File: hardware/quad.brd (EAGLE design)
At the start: 132.1 x 53.3 mm, 18 parts, among them U101 STM32F427VGT6, X101 24MHz

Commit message: Add USB-UART, BNO055
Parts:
- removed J301, J302: (no value), quad:1X50
- added C211, C401, C402, C403, C404: 100nF, quad:C0603
- added C212, C213, C405, C406: 10uF, quad:C0603
- added ESC1, ESC2, ESC3, ESC4: AFRO_ESC, quad:AFRO_ESC
- added IC1: BN055, quad:LGA-28_3.80X5.20/0.5
- added MOT1, MOT2, MOT3, MOT4: MOTOR, quad:MOTOR
- added R101, R401: 10k, quad:R0603
- added R402, R403: 270, quad:R0603
- added RXLED, TXLED: LED, quad:LED-0603
- added U201, U403: LD1117, quad:SOT223
- added U401: FT232R, quad:SSOP28
- added U402: USB-MICROB", quad:USB-B-MICRO-SMD_V03
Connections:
- new net GND_IO: IC1.25
- new net MOT1_1: ESC1.MOT1, MOT1.MOT1
- new net MOT1_2: ESC1.MOT2, MOT1.MOT2
- new net MOT1_3: ESC1.MOT3, MOT1.MOT3
- new net MOT2_1: ESC2.MOT1, MOT2.MOT1
- new net MOT_2_2: ESC2.MOT2, MOT2.MOT2
- new net MOT_2_3: ESC2.MOT3, MOT2.MOT3
- new net MOT_3_1: ESC3.MOT1, MOT3.MOT1
- new net MOT_3_2: ESC3.MOT2, MOT3.MOT2
- new net MOT_3_3: ESC3.MOT3, MOT3.MOT3
- new net MOT_4_1: ESC4.MOT1, MOT4.MOT1
- new net MOT_4_2: ESC4.MOT2, MOT4.MOT2
- new net MOT_4_3: ESC4.MOT3, MOT4.MOT3
- new net N$10: R402.2, RXLED.C
- new net N$11: R403.2, TXLED.C
- new net N$2: R401.1, U401.19
- new net N$5: C401.1, U401.17
- new net N$8: R403.1, U401.23
- new net N$9: R402.1, U401.22
- new net PWM1: ESC1.PWM
- new net PWM2: ESC2.PWM
- new net PWM3: ESC3.PWM
- new net PWM4: ESC4.PWM
- new net USBDM: U401.16, U402.D-
- new net USBDP: U401.15, U402.D+
- new net VBATT: C213.1, ESC1.VBATT, ESC2.VBATT, ESC3.VBATT, ESC4.VBATT, U201.3
- new net VBUS: C402.2, C403.1, C404.1, C405.1, R401.2, U401.20, U403.3
- new net VDD: IC1.3
- new net VDDIO: IC1.28
- net BOOT0: now also U401.2; no longer J302.44
- net BOOT1: now also R101.1; no longer J301.37
- net CAN1_RX: no longer J302.31
- net CAN1_TX: no longer J302.32
- net CAN2_RX: no longer J302.41
- net CAN2_TX: no longer J302.42
- net GND: now also C211.2, C212.2, C213.2, C401.2, C402.1, C403.2, C404.2, C405.2, C406.2, ESC1.GND, ESC1.PWM_GND, ESC2.GND, ESC2.PWM_GND, ESC3.GND, ESC3.PWM_GND, ESC4.GND, ESC4.PWM_GND, IC1.2, R101.2, U201.1, U401.18, U401.21, U401.25, U401.26, U401.7, U402.GND, U403.1; no longer J301.10, J301.11, J301.12, J301.13, J301.19, J301.20, J301.21, J301.22, J301.27, J301.28, J301.49, J301.6, J302.23, J302.24, J302.25, J302.49, J302.50
- net I2C1_SCL: no longer J302.45
- net I2C1_SDA: no longer J302.46
- net I2C2_SCL: no longer J301.47
- net I2C2_SDA: no longer J301.48
- net I2C3_SCL: no longer J302.17
- net I2C3_SDA: no longer J302.16
- net JTCK-SWCLK: no longer J302.26
- net JTDI: no longer J302.27
- net JTDO/TRACESWO: no longer J302.39
- net JTMS-SWDIO: no longer J302.22
- net NJTRST: no longer J302.40
- net NRST: now also U401.3; no longer J301.14
- net PA2: no longer J301.25
- net PA3: no longer J301.26
- net PA4: no longer J301.29
- net PB0: no longer J301.35
- net PB1: no longer J301.36
- net PB12: no longer J302.1
- net PB7: no longer J302.43
- net PC0: no longer J301.15
- net PC1: no longer J301.16
- net PC13: no longer J301.7
- net PC14: no longer J301.8
- net PC15: no longer J301.9
- net PC2: no longer J301.17
- net PC3: no longer J301.18
- net PC4: no longer J301.33
- net PC5: no longer J301.34
- net PC8: no longer J302.15
- net PD10: no longer J302.7
- net PD13: no longer J302.10
- net PD14: no longer J302.11
- net PD15: no longer J302.12
- net PD2: no longer J302.33
- net PD7: no longer J302.38
- net PE10: no longer J301.41
- net PE11: no longer J301.42
- net PE15: no longer J301.46
- net PE2: no longer J301.1
- net PE3: no longer J301.2
- net PE4: no longer J301.3
- net PE5: no longer J301.4
- net PE6: no longer J301.5
- net PE9: no longer J301.40
- net SPI1_MISO: no longer J301.31
- net SPI1_MOSI: no longer J301.32
- net SPI1_SCK: no longer J301.30
- net SPI2_MISO: no longer J302.3
- net SPI2_MOSI: no longer J302.4
- net SPI2_SCK: no longer J302.2
- net SPI3_MISO: no longer J302.29
- net SPI3_MOSI: no longer J302.30
- net SPI3_SCK: no longer J302.28
- net SPI4_MISO: no longer J301.44
- net SPI4_MOSI: no longer J301.45
- net SPI4_SCK: no longer J301.43
- net UART4_RX: no longer J301.24
- net UART4_TX: no longer J301.23
- net UART7_RX: no longer J301.38
- net UART7_TX: no longer J301.39
- net UART8_RX: no longer J302.47
- net UART8_TX: no longer J302.48
- net USART1_CTS: no longer J302.20
- net USART1_RTS: no longer J302.21
- net USART1_RX: now also U401.1; no longer J302.19
- net USART1_TX: now also U401.5; no longer J302.18
- net USART2_CTS: no longer J302.34
- net USART2_RTS: no longer J302.35
- net USART2_RX: no longer J302.37
- net USART2_TX: no longer J302.36
- net USART3_CTS: no longer J302.8
- net USART3_RTS: no longer J302.9
- net USART3_RX: no longer J302.6
- net USART3_TX: no longer J302.5
- net USART6_RX: no longer J302.14
- net USART6_TX: no longer J302.13
- net VDD_3V3: now also C211.1, C212.1, C406.1, RXLED.A, TXLED.A, U201.2, U201.4, U401.4, U403.2, U403.4; no longer J301.50
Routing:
- net VDD_3V3: track 167.9 -> 99.9 mm
- net PB12: track 61.8 -> 0.00 mm
- net PE2: track 61.2 -> 0.00 mm
- net SPI2_SCK: track 59.4 -> 0.00 mm
- net PE3: track 58.9 -> 0.00 mm
- net SPI2_MISO: track 57.1 -> 0.00 mm
- net UART8_TX: track 57.1 -> 0.00 mm
- net I2C2_SDA: track 56.6 -> 0.00 mm
- net PE4: track 56.6 -> 0.00 mm
- net SPI2_MOSI: track 54.8 -> 0.00 mm
- net UART8_RX: track 54.8 -> 0.00 mm
- net BOOT0: track 54.3 -> 0.00 mm, vias 2 -> 0
- net I2C2_SCL: track 54.2 -> 0.00 mm
- net PE5: track 54.2 -> 0.00 mm
- net PC14: track 53.1 -> 0.00 mm, vias 1 -> 0
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- removed copper zone on layer 1, net GND
- removed copper zone on layer 16, net GND
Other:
- board outline removed
- board text removed: "BOOT0"
- board text removed: "BOOT1"
- board text removed: "CAN1_RX"
- board text removed: "CAN1_TX"
- board text removed: "CAN2_RX"
- board text removed: "CAN2_TX"
- board text removed: "GND"
- board text removed: "I2C1_SCL"
- board text removed: "I2C1_SDA"
- board text removed: "I2C2_SCL"
- board text removed: "I2C2_SDA"
- board text removed: "I2C3_SCL"
- board text removed: "I2C3_SDA"
- board text removed: "JTCK-SWCLK"
- board text removed: "JTDI"
- board text removed: "JTDO-TRACESWO"
- board text removed: "JTMS-SWDIO"
- board text removed: "NJTRST"
- board text removed: "NRST"
- board text removed: "PA2"
- board text removed: "PA3"
- board text removed: "PA4"
- board text removed: "PB0"
- board text removed: "PB1"
- board text removed: "PB12"
- board text removed: "PB7"
- board text removed: "PC0"
- board text removed: "PC1"
- board text removed: "PC13"
- board text removed: "PC14"
- board text removed: "PC15"
- board text removed: "PC2"
- board text removed: "PC3"
- board text removed: "PC4"
- board text removed: "PC5"
- board text removed: "PC8"
- board text removed: "PD10"
- board text removed: "PD13"
- board text removed: "PD14"
- board text removed: "PD15"
- board text removed: "PD2"
- board text removed: "PD7"
- board text removed: "PE10"
- board text removed: "PE11"
- board text removed: "PE15"
- board text removed: "PE2"
- board text removed: "PE3"
- board text removed: "PE4"
- board text removed: "PE5"
- board text removed: "PE6"
- board text removed: "PE9"
- board text removed: "SPI1_MISO"
- board text removed: "SPI1_MOSI"
- board text removed: "SPI1_SCK"
- board text removed: "SPI2_MISO"
- board text removed: "SPI2_MOSI"
- board text removed: "SPI2_SCK"
- board text removed: "SPI3_MISO"
- board text removed: "SPI3_MOSI"
- board text removed: "SPI3_SCK"
- board text removed: "SPI4_MISO"
- board text removed: "SPI4_MOSI"
- board text removed: "SPI4_SCK"
- board text removed: "UART4_RX"
- board text removed: "UART4_TX"
- board text removed: "UART7_RX"
- board text removed: "UART7_TX"
- board text removed: "UART8_RX"
- board text removed: "UART8_TX"
- board text removed: "USART1_CTS"
- board text removed: "USART1_RTS"
- board text removed: "USART1_RX"
- board text removed: "USART1_TX"
- board text removed: "USART2_CTS"
- board text removed: "USART2_RTS"
- board text removed: "USART2_RX"
- board text removed: "USART2_TX"
- board text removed: "USART3_CTS"
- board text removed: "USART3_RTS"
- board text removed: "USART3_RX"
- board text removed: "USART3_TX"
- board text removed: "USART6_RX"
- board text removed: "USART6_TX"
- board text removed: "VDD_3V3"

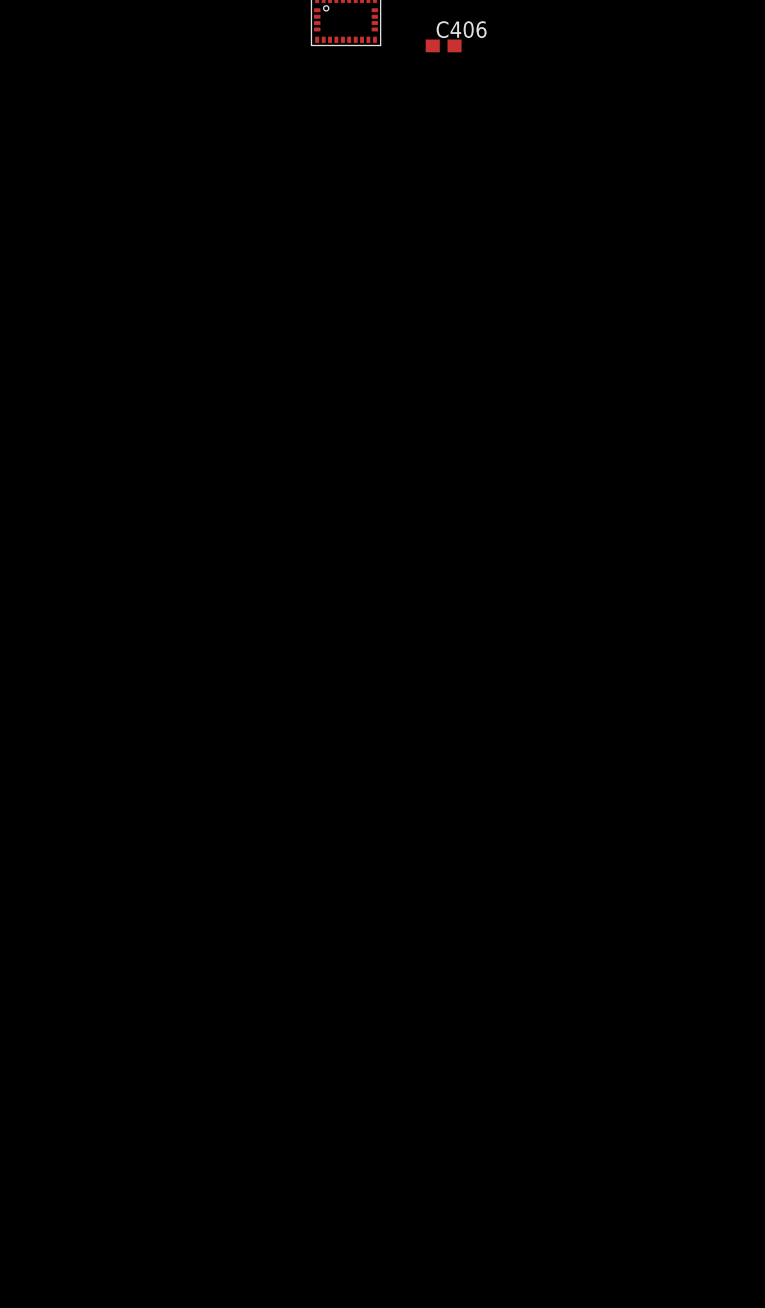
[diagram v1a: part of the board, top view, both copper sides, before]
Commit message: Wire BNO055, Added XBEE
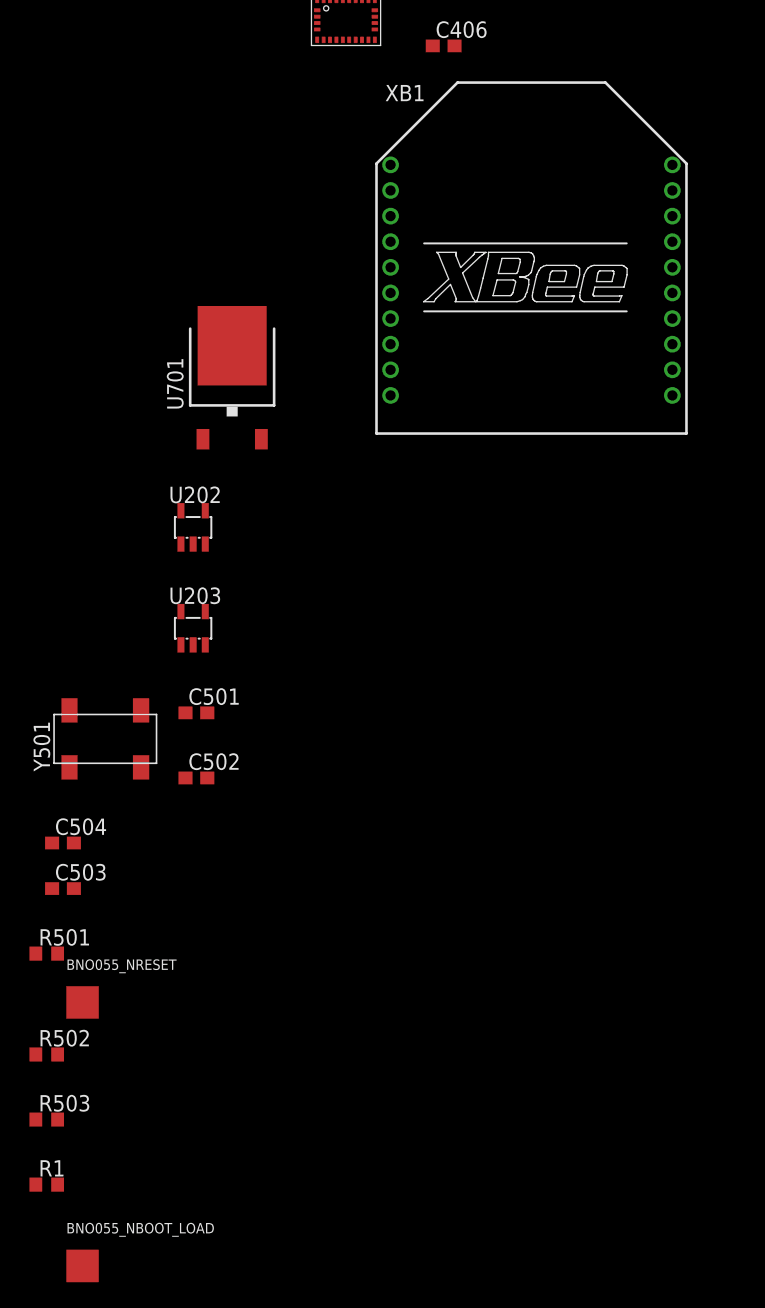
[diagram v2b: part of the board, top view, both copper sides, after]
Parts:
- added BNO055_NBOOT_LOAD, BNO055_NRESET: TESTPAD, quad:TESTPAD
- added C501, C502: 0.1uF, quad:C0603
- added C503, C504: 22pF, quad:C0603
- added R1, R501, R502, R503: 10k, quad:R0603
- added U202, U203: SN74AHC1G32DBVR, quad:SOT23-5L
- added U701: AOD4189, quad:TO252
- added XB1: XBEE, quad:XBEE
- added Y501: 32.768kHz, quad:ABS25
- C404: value 100nF -> 4.7uF
- IC1: value BN055 -> BNO055
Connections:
- removed net GND_IO: IC1.25
- removed net VDD: IC1.3
- removed net VDDIO: IC1.28
- new net FT232_DTR: U203.2, U401.2
- new net FT232_RTS: U202.2, U401.3
- new net N$12: IC1.17, R501.1
- new net N$13: BNO055_NRESET.P$1, IC1.11
- new net N$14: IC1.6, R503.1
- new net N$15: IC1.5, R502.1
- new net N$16: BNO055_NBOOT_LOAD.P$1, IC1.4, R1.1
- new net N$3: U701.3
- new net N$4: C501.2, IC1.9
- new net N$6: C504.2, IC1.27, Y501.4
- new net N$7: C503.2, IC1.26, Y501.1
- new net XBEE_DIO0: U202.1, XB1.20
- new net XBEE_DIO1: U203.1, XB1.19
- new net XBEE_DIO4: XB1.11
- net BOOT0: now also U203.4; no longer U401.2
- net GND: now also C501.1, C502.1, C503.1, C504.1, IC1.10, IC1.15, IC1.16, IC1.18, IC1.25, R501.2, R502.2, R503.2, U202.3, U203.3, XB1.10
- net I2C1_SCL: now also IC1.19
- net I2C1_SDA: now also IC1.20
- net NRST: now also U202.4; no longer U401.3
- net PB12: now also IC1.14
- net USART3_RX: now also XB1.2
- net USART3_TX: now also XB1.3
- net VBATT: now also U701.2
- net VDD_3V3: now also C502.2, IC1.28, IC1.3, R1.2, U202.5, U203.5, XB1.1

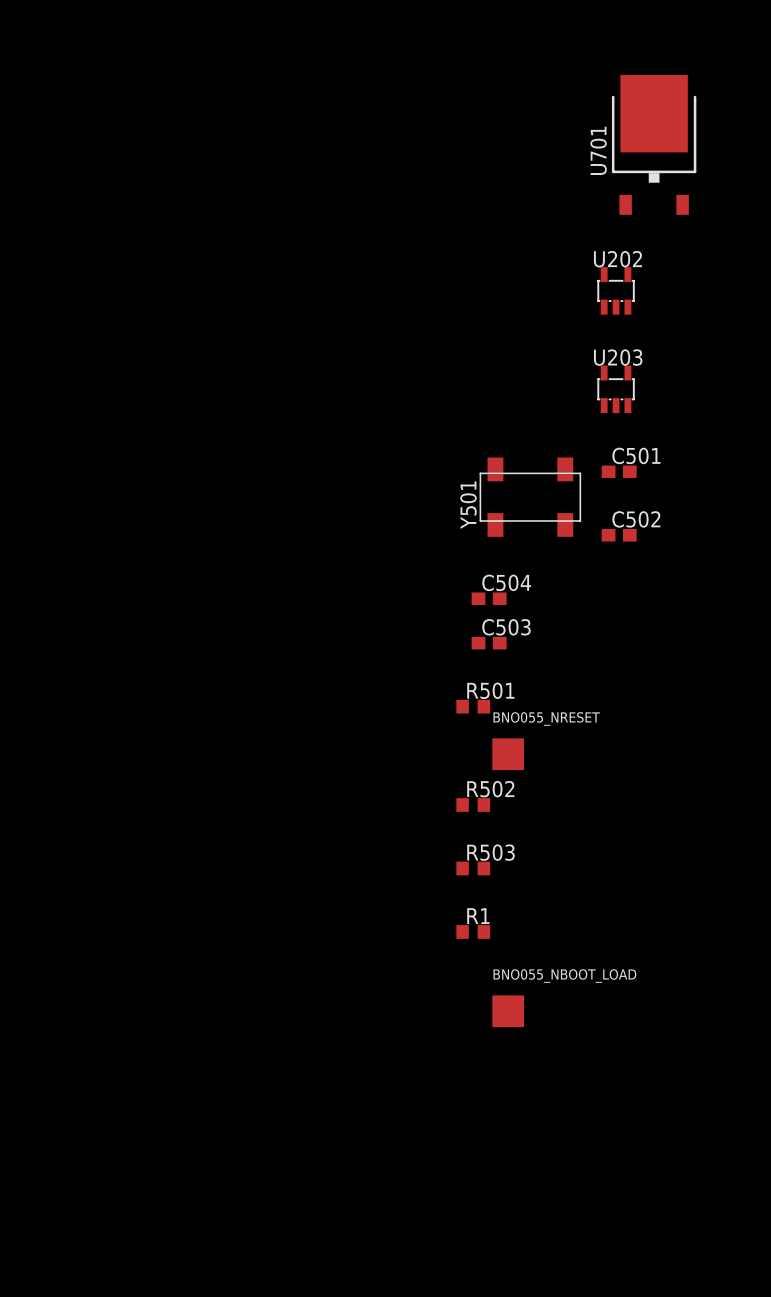
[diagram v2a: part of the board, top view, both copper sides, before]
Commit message: Add power connectors, finish BNO055
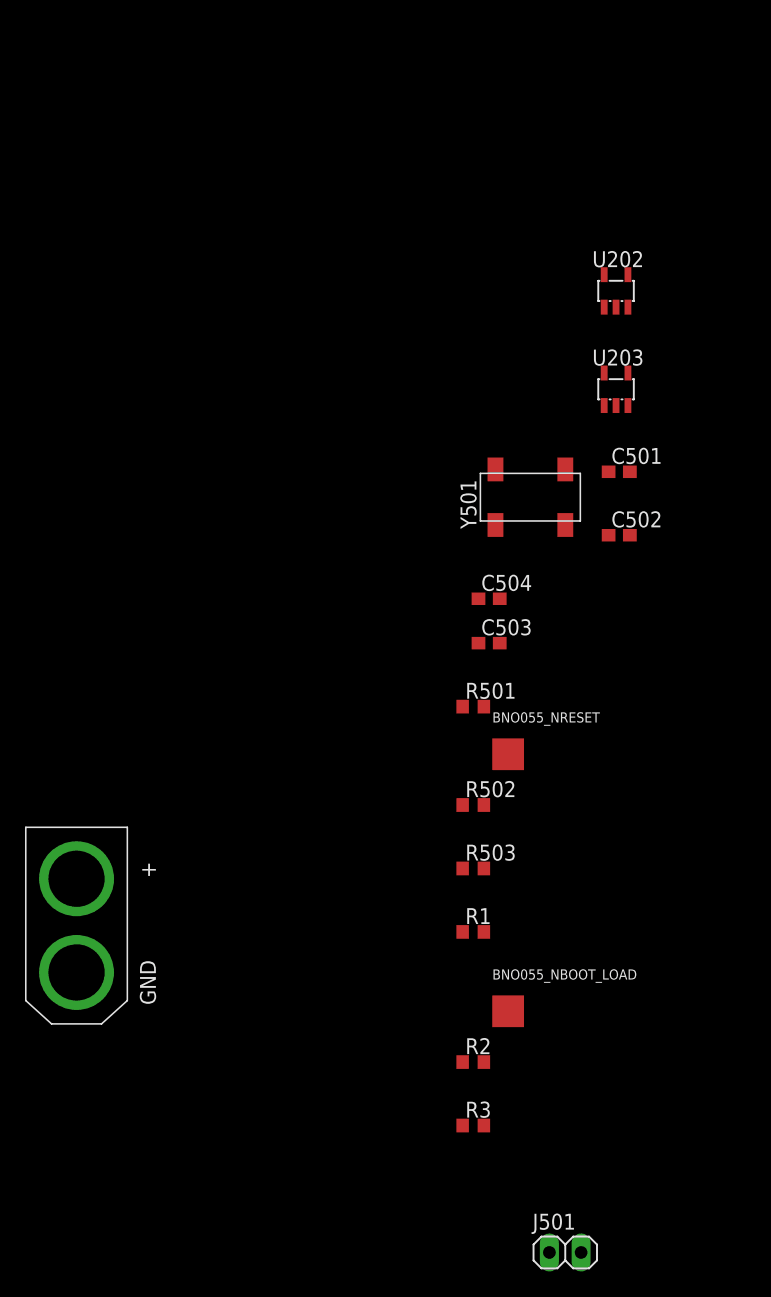
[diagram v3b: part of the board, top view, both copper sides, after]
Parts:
- removed U701: AOD4189, quad:TO252
- added J501: I2C_TEST, quad:1X02
- added R2, R3: 10k, quad:R0603
- added U$1: XT60, quad:XT60
- U202: value SN74AHC1G32DBVR -> AND_GATE
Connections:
- net SPI3_MOSI renamed PC12
- net USART3_CTS renamed PD11
- net USART3_RTS renamed PD12
- removed net SPI3_MISO: U101.79
- removed net SPI3_SCK: U101.78
- new net PD8: U101.55
- new net PD9: U101.56
- net GND: now also U$1.GND
- net I2C1_SCL: now also J501.2, R3.2
- net I2C1_SDA: now also J501.1, R2.2
- net N$3: now also U$1.PWR; no longer U701.3
- net USART3_RX: now also U101.79; no longer U101.56
- net USART3_TX: now also U101.78; no longer U101.55
- net VBATT: no longer U701.2
- net VDD_3V3: now also R2.1, R3.1
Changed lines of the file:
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@@
 <attribute name="OC_NEWARK" value="34R5507" x="-236.982" y="-274.32" size="1.778" layer="27" display="off"/>
 </element>
-<element name="U701" library="quad" package="TO252" value="AOD4189" x="-260.35" y="-281.94"/>
-<element name="U202" library="quad" package="SOT23-5L" value="SN74AHC1G32DBVR" x="-263.398" y="-293.624"/>
+<element name="U202" library="quad" package="SOT23-5L" value="AND_GATE" x="-263.398" y="-293.624"/>
 <element name="U203" library="quad" package="SOT23-5L" value="SN74AHC1G32DBVR" x="-263.398" y="-301.498"/>
 <element name="C501" library="quad" package="C0603" value="0.1uF" x="-263.144" y="-308.102"/>
@@
 <element name="R1" library="quad" package="R0603" value="10k" x="-274.828" y="-344.932"/>
 <element name="BNO055_NBOOT_LOAD" library="quad" package="TESTPAD" value="TESTPAD" x="-272.034" y="-351.282"/>
+<element name="R2" library="quad" package="R0603" value="10k" x="-274.828" y="-355.346"/>
+<element name="R3" library="quad" package="R0603" value="10k" x="-274.828" y="-360.426"/>
+<element name="J501" library="quad" package="1X02" value="I2C_TEST" x="-267.462" y="-370.586"/>
+<element name="U$1" library="quad" package="XT60" value="XT60" x="-306.578" y="-344.424"/>
 </elements>
 <signals>
@@
 <contactref element="R502" pad="2"/>
 <contactref element="R503" pad="2"/>
+<contactref element="U$1" pad="GND"/>
 <wire x1="-249.21" y1="-255.56" x2="-251.71" y2="-255.56" width="0" layer="19" extent="1-1"/>
 <wire x1="-249.21" y1="-254.75" x2="-249.21" y2="-255.56" width="0" layer="19" extent="1-1"/>
@@
 <wire x1="-273.978" y1="-334.772" x2="-273.978" y2="-326.898" width="0" layer="19" extent="1-1"/>
 <wire x1="-273.978" y1="-339.852" x2="-273.978" y2="-334.772" width="0" layer="19" extent="1-1"/>
+<wire x1="-306.578" y1="-348.174" x2="-273.978" y2="-339.852" width="0" layer="19" extent="1-1"/>
 <wire x1="-208.026" y1="91.186" x2="-223.68" y2="-167.946" width="0" layer="19" extent="1-1"/>
 <wire x1="-195.326" y1="95.631" x2="-208.026" y2="91.186" width="0" layer="19" extent="1-1"/>
@@
 <contactref element="U101" pad="95"/>
 <contactref element="IC1" pad="19"/>
+<contactref element="R3" pad="2"/>
+<contactref element="J501" pad="2"/>
+<wire x1="-273.978" y1="-360.426" x2="-249.21" y2="-253.25" width="0" layer="19" extent="1-1"/>
+<wire x1="-266.192" y1="-370.586" x2="-273.978" y2="-360.426" width="0" layer="19" extent="1-1"/>
 <wire x1="58.105128125" y1="30.290121875" x2="-249.21" y2="-253.25" width="0" layer="19" extent="1-1"/>
 </signal>
 <signal name="I2C1_SDA">
 <contactref element="U101" pad="96"/>
+<contactref element="J501" pad="1"/>
 <contactref element="IC1" pad="20"/>
+<contactref element="R2" pad="2"/>
+<wire x1="-273.978" y1="-355.346" x2="-249.21" y2="-252.44" width="0" layer="19" extent="1-1"/>
+<wire x1="-268.732" y1="-370.586" x2="-273.978" y2="-355.346" width="0" layer="19" extent="1-1"/>
 <wire x1="57.751575" y1="29.936565625" x2="-249.21" y2="-252.44" width="0" layer="19" extent="1-1"/>
 </signal>
@@
 <contactref element="U101" pad="66"/>
 </signal>
-<signal name="SPI3_SCK">
-<contactref element="U101" pad="78"/>
-</signal>
-<signal name="SPI3_MISO">
-<contactref element="U101" pad="79"/>
-</signal>
-<signal name="SPI3_MOSI">
+<signal name="PC12">
 <contactref element="U101" pad="80"/>
 </signal>
@@
 </signal>
 <signal name="USART3_TX">
-<contactref element="U101" pad="55"/>
 <contactref element="XB1" pad="3"/>
-<wire x1="-247.982" y1="-269.32" x2="74.328421875" y2="29.936565625" width="0" layer="19" extent="1-1"/>
+<contactref element="U101" pad="78"/>
+<wire x1="-247.982" y1="-269.32" x2="64.1155375" y2="36.300528125" width="0" layer="19" extent="1-1"/>
 </signal>
 <signal name="USART3_RX">
-<contactref element="U101" pad="56"/>
 <contactref element="XB1" pad="2"/>
-<wire x1="-247.982" y1="-267.32" x2="73.97486875" y2="30.290121875" width="0" layer="19" extent="1-1"/>
+<contactref element="U101" pad="79"/>
+<wire x1="-247.982" y1="-267.32" x2="63.761984375" y2="35.946975" width="0" layer="19" extent="1-1"/>
 </signal>
 <signal name="PD10">
 <contactref element="U101" pad="57"/>
 </signal>
-<signal name="USART3_CTS">
+<signal name="PD11">
 <contactref element="U101" pad="58"/>
 </signal>
-<signal name="USART3_RTS">
+<signal name="PD12">
 <contactref element="U101" pad="59"/>
 </signal>
@@
 <contactref element="C502" pad="2"/>
 <contactref element="R1" pad="2"/>
+<contactref element="R3" pad="1"/>
+<contactref element="R2" pad="1"/>
 <wire x1="-253.21" y1="-252.44" x2="-253.71" y2="-253.75" width="0" layer="19" extent="1-1"/>
 <wire x1="-244.69" y1="-256.032" x2="-253.21" y2="-252.44" width="0" layer="19" extent="1-1"/>
@@
 <wire x1="-262.294" y1="-313.182" x2="-264.348" y2="-300.198" width="0" layer="19" extent="1-1"/>
 <wire x1="-273.978" y1="-344.932" x2="-262.294" y2="-313.182" width="0" layer="19" extent="1-1"/>
+<wire x1="-275.678" y1="-355.346" x2="-273.978" y2="-344.932" width="0" layer="19" extent="1-1"/>
+<wire x1="-275.678" y1="-360.426" x2="-275.678" y2="-355.346" width="0" layer="19" extent="1-1"/>
 <wire x1="36.83" y1="12.534" x2="-220.98" y2="-161.746" width="0" layer="19" extent="1-1"/>
 <wire x1="49.784" y1="22.44" x2="36.83" y2="12.534" width="0" layer="19" extent="1-1"/>
@@
 <contactref element="C213" pad="1"/>
 <contactref element="U201" pad="3"/>
-<contactref element="U701" pad="2"/>
 <wire x1="-218.28" y1="-167.946" x2="-228.688" y2="-173.736" width="0" layer="19" extent="1-1"/>
-<wire x1="-258.07" y1="-286.74" x2="-228.688" y2="-173.736" width="0" layer="19" extent="1-1"/>
 <wire x1="-187.706" y1="91.186" x2="-218.28" y2="-167.946" width="0" layer="19" extent="1-1"/>
 <wire x1="-122.174" y1="91.186" x2="-187.706" y2="91.186" width="0" layer="19" extent="1-1"/>
@@
 </signal>
 <signal name="N$3">
-<contactref element="U701" pad="3"/>
+<contactref element="U$1" pad="PWR"/>
 </signal>
 <signal name="XBEE_DIO4">
@@
 <wire x1="-272.034" y1="-351.282" x2="-275.678" y2="-344.932" width="0" layer="19" extent="1-1"/>
 </signal>
+<signal name="PD9">
+<contactref element="U101" pad="56"/>
+</signal>
+<signal name="PD8">
+<contactref element="U101" pad="55"/>
+</signal>
 </signals>
